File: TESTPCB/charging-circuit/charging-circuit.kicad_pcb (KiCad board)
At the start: 2 copper layers, 82.6 x 94.6 mm, 335 parts, among them J1 2.54-1*6PHeader-RA, J10 Conn_01x02, J11 Conn_01x04, J2 USB_C_Receptacle_PowerOnly_6P, P1 Header-Male-2.54_2x2, P10 1.27mm/1*3p, P11 1.27mm/1*3p, P2 Header-Male-2.54_2x2, P3 1.27mm/1*3p, P4 1.27mm/1*3p, P5 1.27mm/1*3p, P6 1.27mm/1*3p, P7 1.27mm/1*3p, P8 1.27mm/1*3p, P9 1.27mm/1*3p, Q1 2N7002, Q10 AO3400A, Q11 AO3401A, Q2 CJQ4435, Q3 currentmirror, Q4 BSS84, Q5 AO4892, Q6 AO3401A, Q7 AO3401A, Q8 CJQ4435, Q9 AO3400A, SW1 TS-1088R-02026, U1 MAX17048G+T10, U10 BQ25606RGER, U11 Battery Input, U12 BQ24170RGYR, U13 TPS54302DDCR_C311983, U14 NTC10K/0805/F, U15 BQ76920PW, U16 NTC10K/0805/F, U17 HUSB238_002DD, U19 TPS54302DDCR_C311983, U2 MT3608, U20 TPS54302DDCR_C311983, U21 MCP73871, U3 MT3608, U4 TPL5110DDCT, U5 BQ25606RGER, U6 MT3608, U7 Z-21320110021001, U8 MAX3232CDBR, U9 ADS1115IDGSR

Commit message: fixed board layout
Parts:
- removed L4: SDFL2012Q1R0KTF, easyeda2kicad:L0805
- added D14: SS14, PCM_JLCPCB:D_SMA, F.Cu at (49.8, 66.8)
- added U22: SRP4020TA-1R0M, easyeda2kicad:IND-SMD_L4.5-W4.1_SRP4020TA, F.Cu at (61.1, 69.8)
- moved C13 1.11 mm to (56.0, 69.3)
- moved C14 1.11 mm to (58.8, 77.0)
- moved C15 1.11 mm to (55.8, 71.5)
- moved C16 1.11 mm to (58.0, 73.0)
- moved C22 1.11 mm to (58.8, 75.5)
- moved C9 1.11 mm to (52.3, 70.3)
- moved D8 1.11 mm to (52.8, 83.0)
- moved D9 1.11 mm to (56.0, 83.8)
- moved H3 1.11 mm to (49.0, 77.0)
- moved R17 1.11 mm to (52.5, 80.0)
- moved R22 1.11 mm to (57.8, 81.0)
- moved R24 1.11 mm to (54.8, 81.0)
- moved R25 1.11 mm to (56.3, 81.0)
- moved R27 1.11 mm to (61.0, 76.3)
- moved R28 1.11 mm to (60.5, 78.8)
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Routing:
- net /VBUS1: track 7.66 -> 15.7 mm, vias 0 -> 2
- net /GND1: track 62.7 -> 64.8 mm
- net Net-(C16-Pad2): track 8.25 -> 10.1 mm

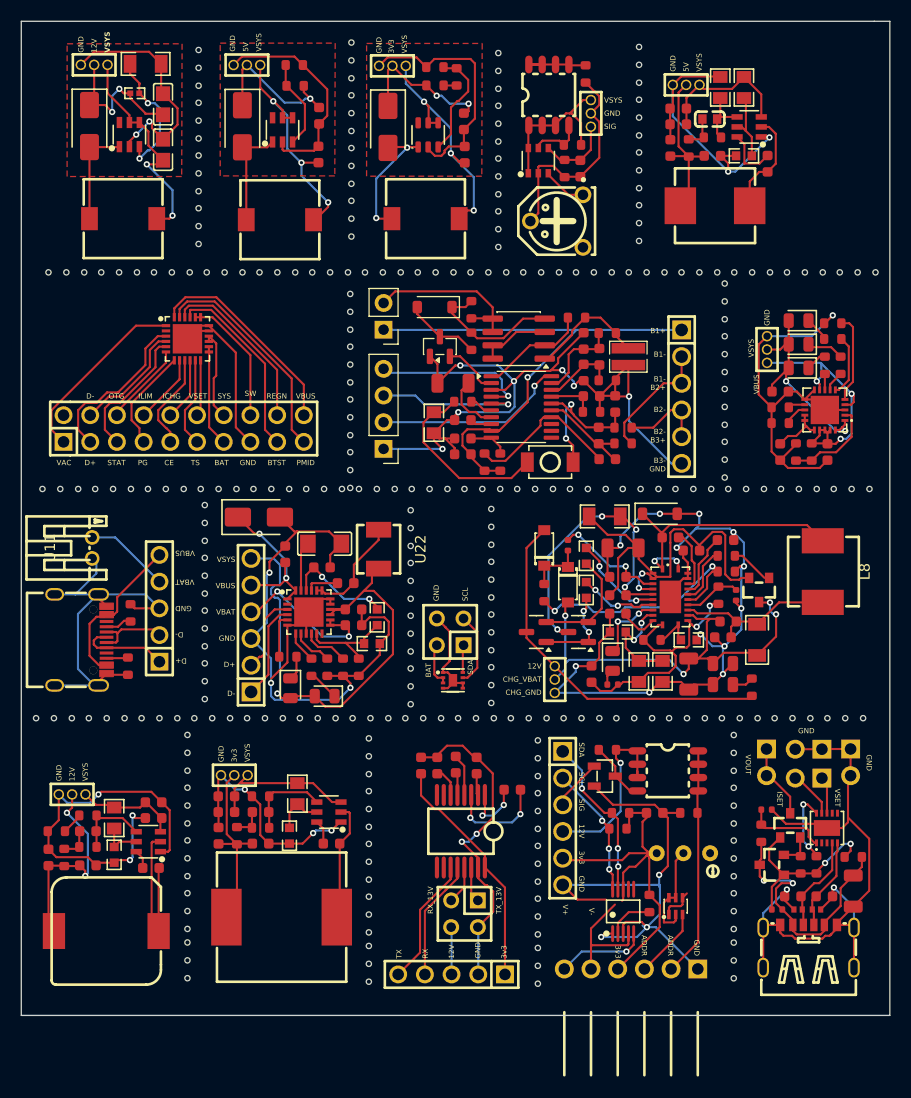
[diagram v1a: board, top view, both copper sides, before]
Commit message: Mouse Holes replaced with Break Tabs
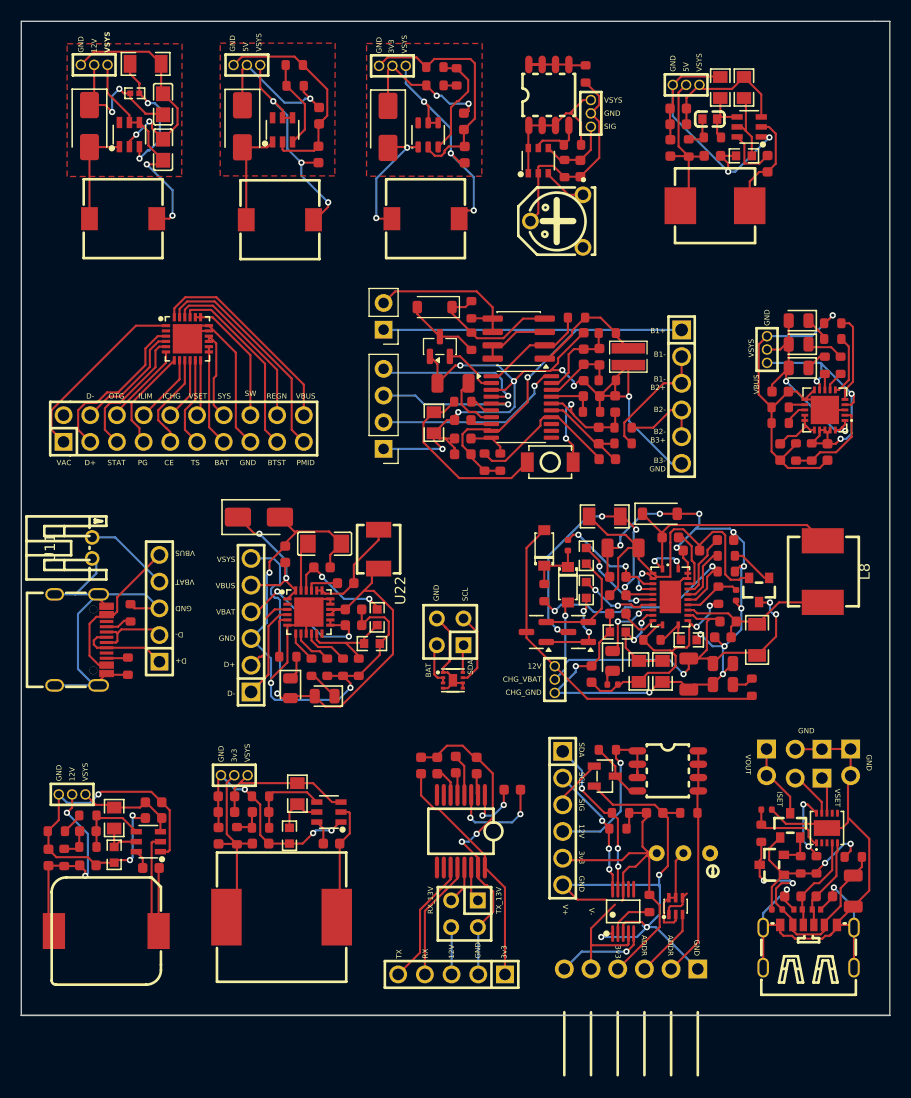
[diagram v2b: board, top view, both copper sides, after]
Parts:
- removed REF** (x104): BreakLine_3h_D0.5mm_P1.7mm, MouseBites:BreakLine_3h_D0.5mm_P1.7mm
- added ?: , , F.Cu at (54.3, 64.3)
- added ?: , , F.Cu at (41.3, 64.3)
- added ?: , , F.Cu at (31.0, 43.5)
- added ?: , , F.Cu at (93.5, 85.7)
- added ?: , , F.Cu at (67.5, 85.7)
- added ?: , , F.Cu at (104.8, 64.3)
- added ?: , , F.Cu at (67.5, 43.5)
- added ?: , , F.Cu at (57.7, 53.9)
- added ?: , , F.Cu at (60.1, 92.6)
- added ?: , , F.Cu at (76.2, 92.6)
- added ?: , , F.Cu at (94.0, 53.9)
- added ?: , , F.Cu at (72.0, 74.8)
- added ?: , , F.Cu at (105.0, 85.7)
- added ? (x2): , , F.Cu at (72.7, 31.4)
- added ?: , , F.Cu at (58.5, 31.5)
- added ?: , , F.Cu at (80.5, 43.5)
- added ?: , , F.Cu at (87.0, 31.4)
- added ?: , , F.Cu at (93.3, 64.3)
- added ?: , , F.Cu at (43.0, 106.7)
- added ?: , , F.Cu at (54.5, 85.7)
- added ?: , , F.Cu at (94.5, 93.0)
- added ?: , , F.Cu at (41.5, 85.7)
- added ?: , , F.Cu at (80.5, 85.7)
- added ?: , , F.Cu at (44.1, 31.6)
- added ?: , , F.Cu at (93.5, 43.5)
- added ?: , , F.Cu at (44.5, 74.8)
- added ?: , , F.Cu at (43.0, 92.7)
- added ?: , , F.Cu at (67.3, 64.3)
- added ?: , , F.Cu at (94.5, 107.0)
- added ?: , , F.Cu at (105.0, 43.5)
- added ?: , , F.Cu at (30.8, 64.3)
- added ?: , , F.Cu at (60.1, 106.6)
- added ?: , , F.Cu at (64.5, 74.8)
- added ?: , , F.Cu at (41.5, 43.5)
- added ?: , , F.Cu at (76.2, 106.6)
- added ?: , , F.Cu at (31.0, 85.7)
- added ?: , , F.Cu at (80.3, 64.3)
- added ?: , , F.Cu at (54.5, 43.5)

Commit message: fixed drc
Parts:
- removed the ? at (72.7, 31.4)
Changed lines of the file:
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@@
 	(footprint ""
 		(layer "F.Cu")
-		(at 72.675 31.45 90)
-		(property "Reference" ""
-			(at 0 0 90)
-			(layer "F.SilkS")
-			(effects
-				(font
-					(size 1.27 1.27)
-					(thickness 0.15)
-				)
-			)
-		)
-		(property "Value" ""
-			(at 0 0 90)
-			(layer "F.Fab")
-			(effects
-				(font
-					(size 1.27 1.27)
-					(thickness 0.15)
-				)
-			)
-		)
-		(property "Datasheet" ""
-			(at 0 0 90)
-			(layer "F.Fab")
-			(hide yes)
-			(effects
-				(font
-					(size 1.27 1.27)
-					(thickness 0.15)
-				)
-			)
-		)
-		(property "Description" ""
-			(at 0 0 90)
-			(layer "F.Fab")
-			(hide yes)
-			(effects
-				(font
-					(size 1.27 1.27)
-					(thickness 0.15)
-				)
-			)
-		)
-		(pad "" np_thru_hole circle
-			(at 0 0 180)
-			(size 0.5 0.5)
-			(drill oval 0.5 23)
-			(layers "*.Cu" "*.Mask")
-		)
-		(embedded_fonts no)
-	)
-	(footprint ""
-		(layer "F.Cu")
 		(at 58.525 31.5 90)
 		(property "Reference" ""
@@
 		(stroke
 			(width 0.05)
-			(type default)
-		)
-		(layer "Edge.Cuts")
-	)
-	(gr_line
-		(start 109.79 114.18)
-		(end 27.15 114.18)
-		(stroke
-			(width 0.05)
